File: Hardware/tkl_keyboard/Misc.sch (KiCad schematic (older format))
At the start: 16 parts, among them J6 Conn_01x04_Female, SW90 Rotary_Encoder_Switch, SW91 Rotary_Encoder_Switch, SW92 Rotary_Encoder_Switch

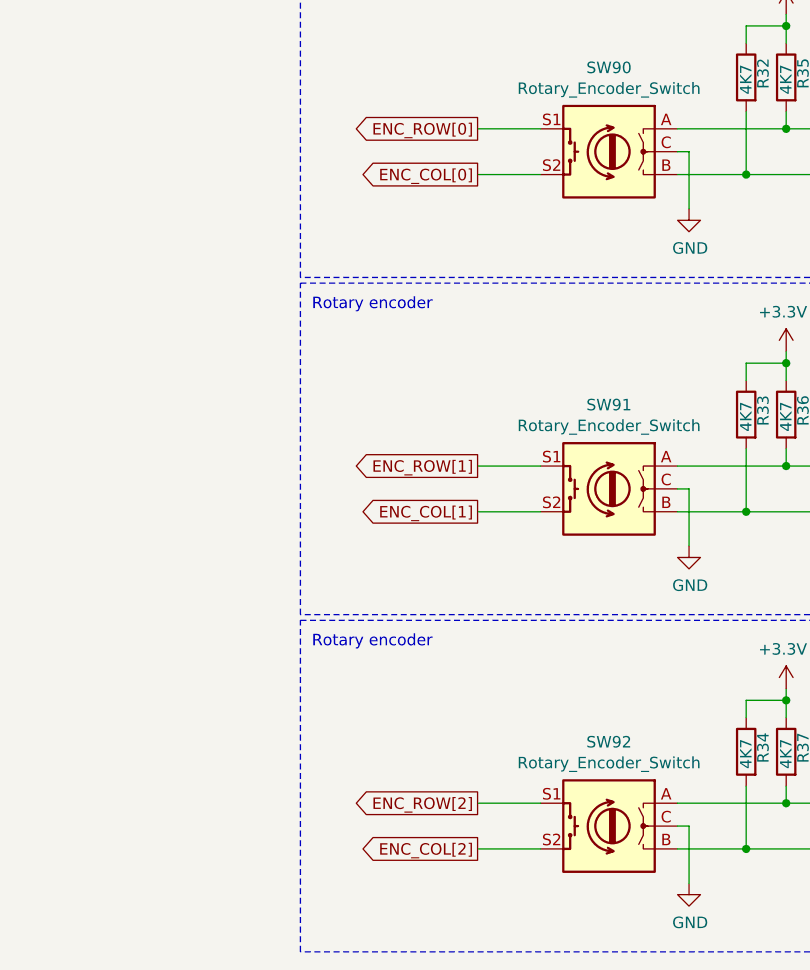
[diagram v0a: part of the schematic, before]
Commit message: LEDs and diodes routed
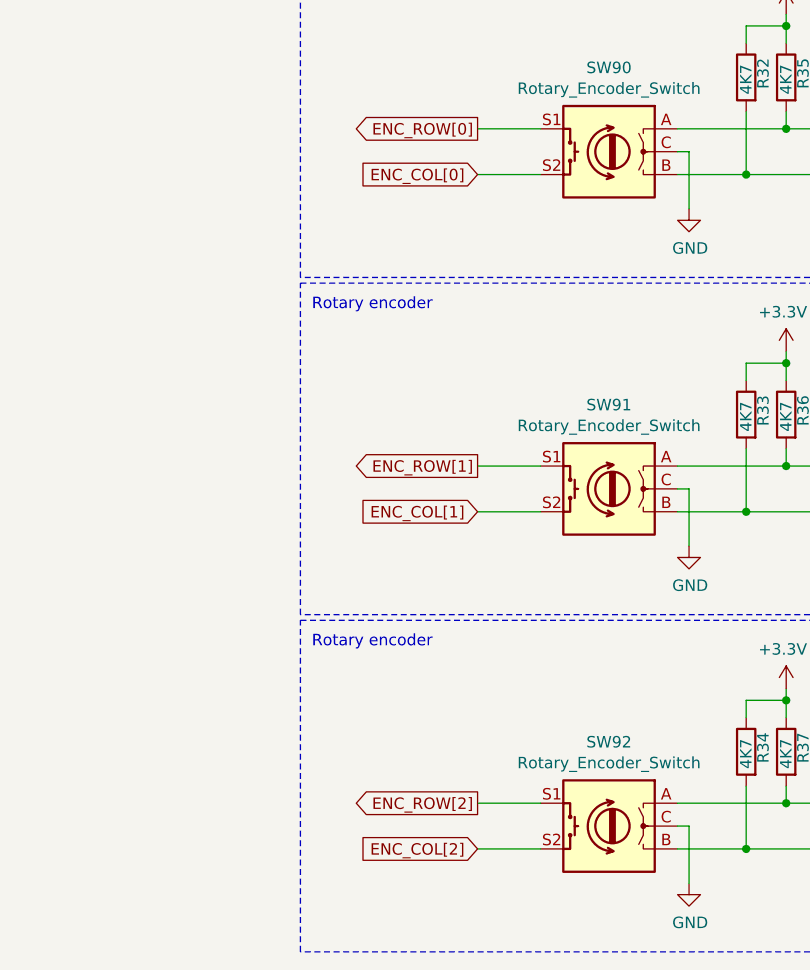
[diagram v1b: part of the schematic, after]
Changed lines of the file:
@@
 Text GLabel 4025 2550 0    50   Output ~ 0
 ENC_ROW[0]
-Text GLabel 4025 2750 0    50   Output ~ 0
+Text GLabel 4025 2750 0    50   Input ~ 0
 ENC_COL[0]
 Wire Wire Line
@@
 Text GLabel 4025 4025 0    50   Output ~ 0
 ENC_ROW[1]
-Text GLabel 4025 4225 0    50   Output ~ 0
+Text GLabel 4025 4225 0    50   Input ~ 0
 ENC_COL[1]
 Wire Wire Line
@@
 Text GLabel 4025 5500 0    50   Output ~ 0
 ENC_ROW[2]
-Text GLabel 4025 5700 0    50   Output ~ 0
+Text GLabel 4025 5700 0    50   Input ~ 0
 ENC_COL[2]
 Wire Wire Line

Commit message: Rows and columns routed to controller. Extended top board edge to fit OLED. Removed optional resistors around CMC.
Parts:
- J6: footprint Connector_PinSocket_2.54mm:PinSocket_1x04_P2.54mm_Vertical -> custom_footprint_library:OLED_128_64
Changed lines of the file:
@@
 F 0 "J6" H 7628 3676 50  0000 L CNN
 F 1 "Conn_01x04_Female" H 7300 3400 50  0000 L CNN
-F 2 "Connector_PinSocket_2.54mm:PinSocket_1x04_P2.54mm_Vertical" H 7600 3700 50  0001 C CNN
+F 2 "custom_footprint_library:OLED_128_64" H 7600 3700 50  0001 C CNN
 F 3 "~" H 7600 3700 50  0001 C CNN
 	1    7600 3700

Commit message: Updating schematic
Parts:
- added H10, H11, H12, H5, H6, H7, H8, H9: MountingHole_Pad, mounting_hole:MountingHole_3.2mm_M3_ISO7380_Pad, symbol Mechanical:MountingHole_Pad
- R32, R33, R34, R35, R36, R37: value 4K7 -> 10K
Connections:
- net GND: now also H10.1, H11.1, H12.1, H5.1, H6.1, H7.1, H8.1, H9.1
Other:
- moved on the sheet: H1, H2, H3, H4, J6, R30, R31, R32, R33, R34, R35, R36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

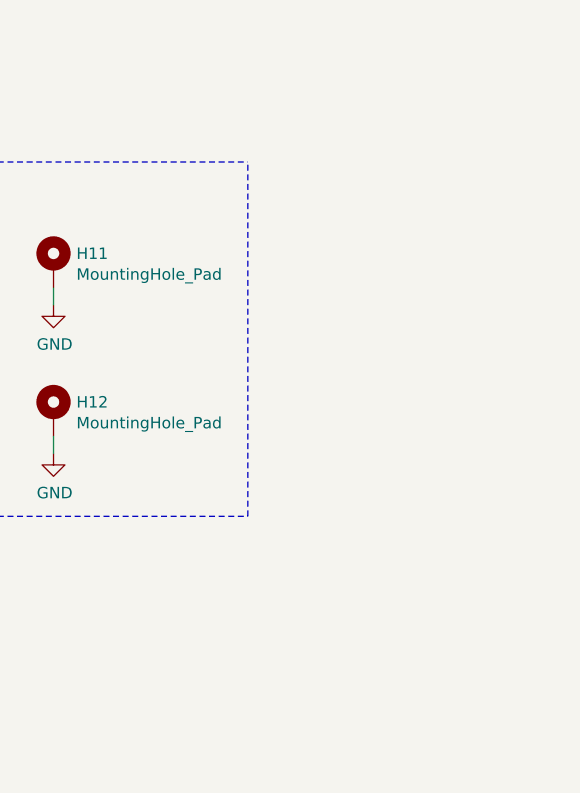
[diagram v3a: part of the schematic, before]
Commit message: First pass of routing done
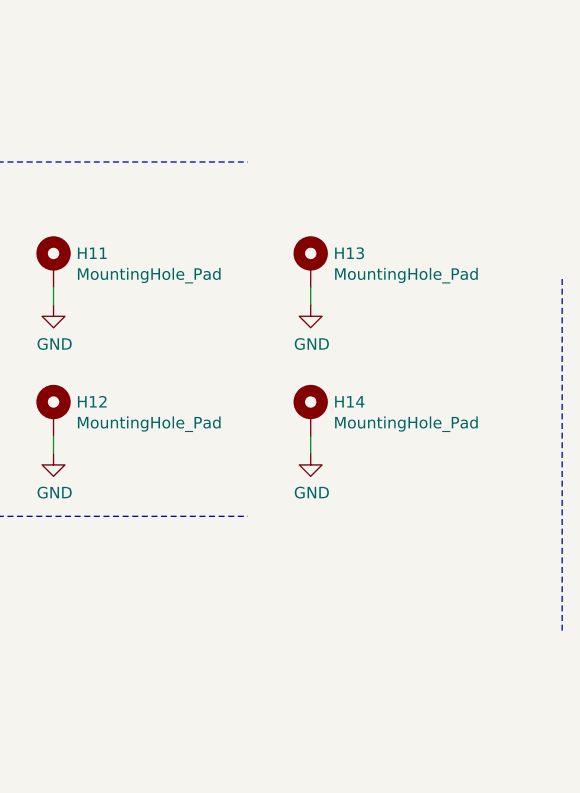
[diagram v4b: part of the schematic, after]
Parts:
- added H13, H14: MountingHole_Pad, mounting_hole:MountingHole_3.2mm_M3_ISO7380_Pad, symbol Mechanical:MountingHole_Pad
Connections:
- net GND: now also H13.1, H14.1
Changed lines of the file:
@@
 	1750 3050 7925 3050
 Wire Notes Line
-	7925 3050 7925 1500
+	9300 3550 9300 2000
 Wire Notes Line
 	1750 1500 7925 1500
+$Comp
+L Mechanical:MountingHole_Pad H?
+U 1 1 61422488
+P 8200 1950
+AR Path="/62F5643B/61422488" Ref="H?"  Part="1"
+AR Path="/63013830/61422488" Ref="H?"  Part="1"
+AR Path="/6301FD9D/61422488" Ref="H?"  Part="1"
+AR Path="/63166CC9/61422488" Ref="H13"  Part="1"
+F 0 "H13" H 8300 1999 50  0000 L CNN
+F 1 "MountingHole_Pad" H 8300 1908 50  0000 L CNN
+F 2 "mounting_hole:MountingHole_3.2mm_M3_ISO7380_Pad" H 8200 1950 50  0001 C CNN
+F 3 "~" H 8200 1950 50  0001 C CNN
+	1    8200 1950
+	1    0    0    -1
+$EndComp
+$Comp
+L power:GND #PWR?
+U 1 1 6142248E
+P 8200 2125
+AR Path="/62F5643B/6142248E" Ref="#PWR?"  Part="1"
+AR Path="/63013830/6142248E" Ref="#PWR?"  Part="1"
+AR Path="/6301FD9D/6142248E" Ref="#PWR?"  Part="1"
+AR Path="/63166CC9/6142248E" Ref="#PWR0529"  Part="1"
+F 0 "#PWR0529" H 8200 1875 50  0001 C CNN
+F 1 "GND" H 8205 1952 50  0000 C CNN
+F 2 "" H 8200 2125 50  0001 C CNN
+F 3 "" H 8200 2125 50  0001 C CNN
+	1    8200 2125
+	1    0    0    -1
+$EndComp
+Wire Wire Line
+	8200 2125 8200 2050
+$Comp
+L Mechanical:MountingHole_Pad H?
+U 1 1 61422495
+P 8200 2600
+AR Path="/62F5643B/61422495" Ref="H?"  Part="1"
+AR Path="/63013830/61422495" Ref="H?"  Part="1"
+AR Path="/6301FD9D/61422495" Ref="H?"  Part="1"
+AR Path="/63166CC9/61422495" Ref="H14"  Part="1"
+F 0 "H14" H 8300 2649 50  0000 L CNN
+F 1 "MountingHole_Pad" H 8300 2558 50  0000 L CNN
+F 2 "mounting_hole:MountingHole_3.2mm_M3_ISO7380_Pad" H 8200 2600 50  0001 C CNN
+F 3 "~" H 8200 2600 50  0001 C CNN
+	1    8200 2600
+	1    0    0    -1
+$EndComp
+$Comp
+L power:GND #PWR?
+U 1 1 6142249B
+P 8200 2775
+AR Path="/62F5643B/6142249B" Ref="#PWR?"  Part="1"
+AR Path="/63013830/6142249B" Ref="#PWR?"  Part="1"
+AR Path="/6301FD9D/6142249B" Ref="#PWR?"  Part="1"
+AR Path="/63166CC9/6142249B" Ref="#PWR0530"  Part="1"
+F 0 "#PWR0530" H 8200 2525 50  0001 C CNN
+F 1 "GND" H 8205 2602 50  0000 C CNN
+F 2 "" H 8200 2775 50  0001 C CNN
+F 3 "" H 8200 2775 50  0001 C CNN
+	1    8200 2775
+	1    0    0    -1
+$EndComp
+Wire Wire Line
+	8200 2775 8200 2700
 $EndSCHEMATC

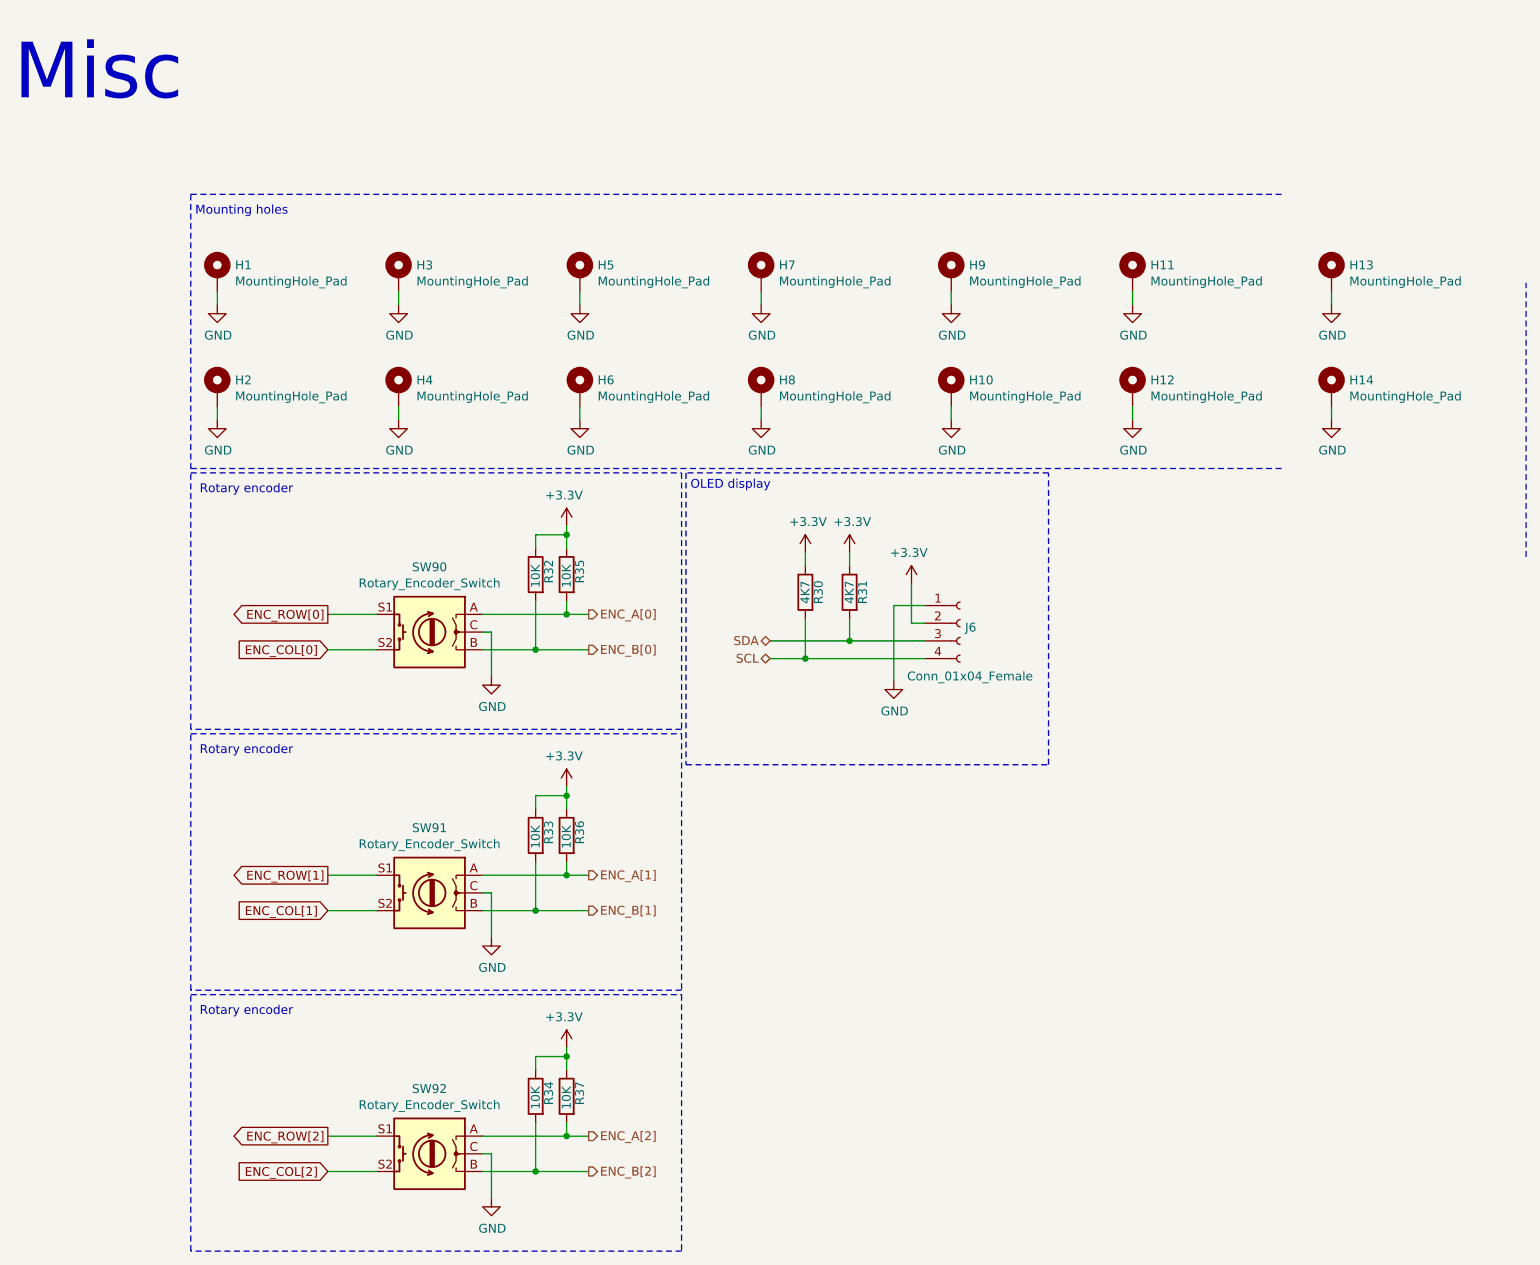
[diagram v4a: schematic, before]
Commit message: Tidying schematic
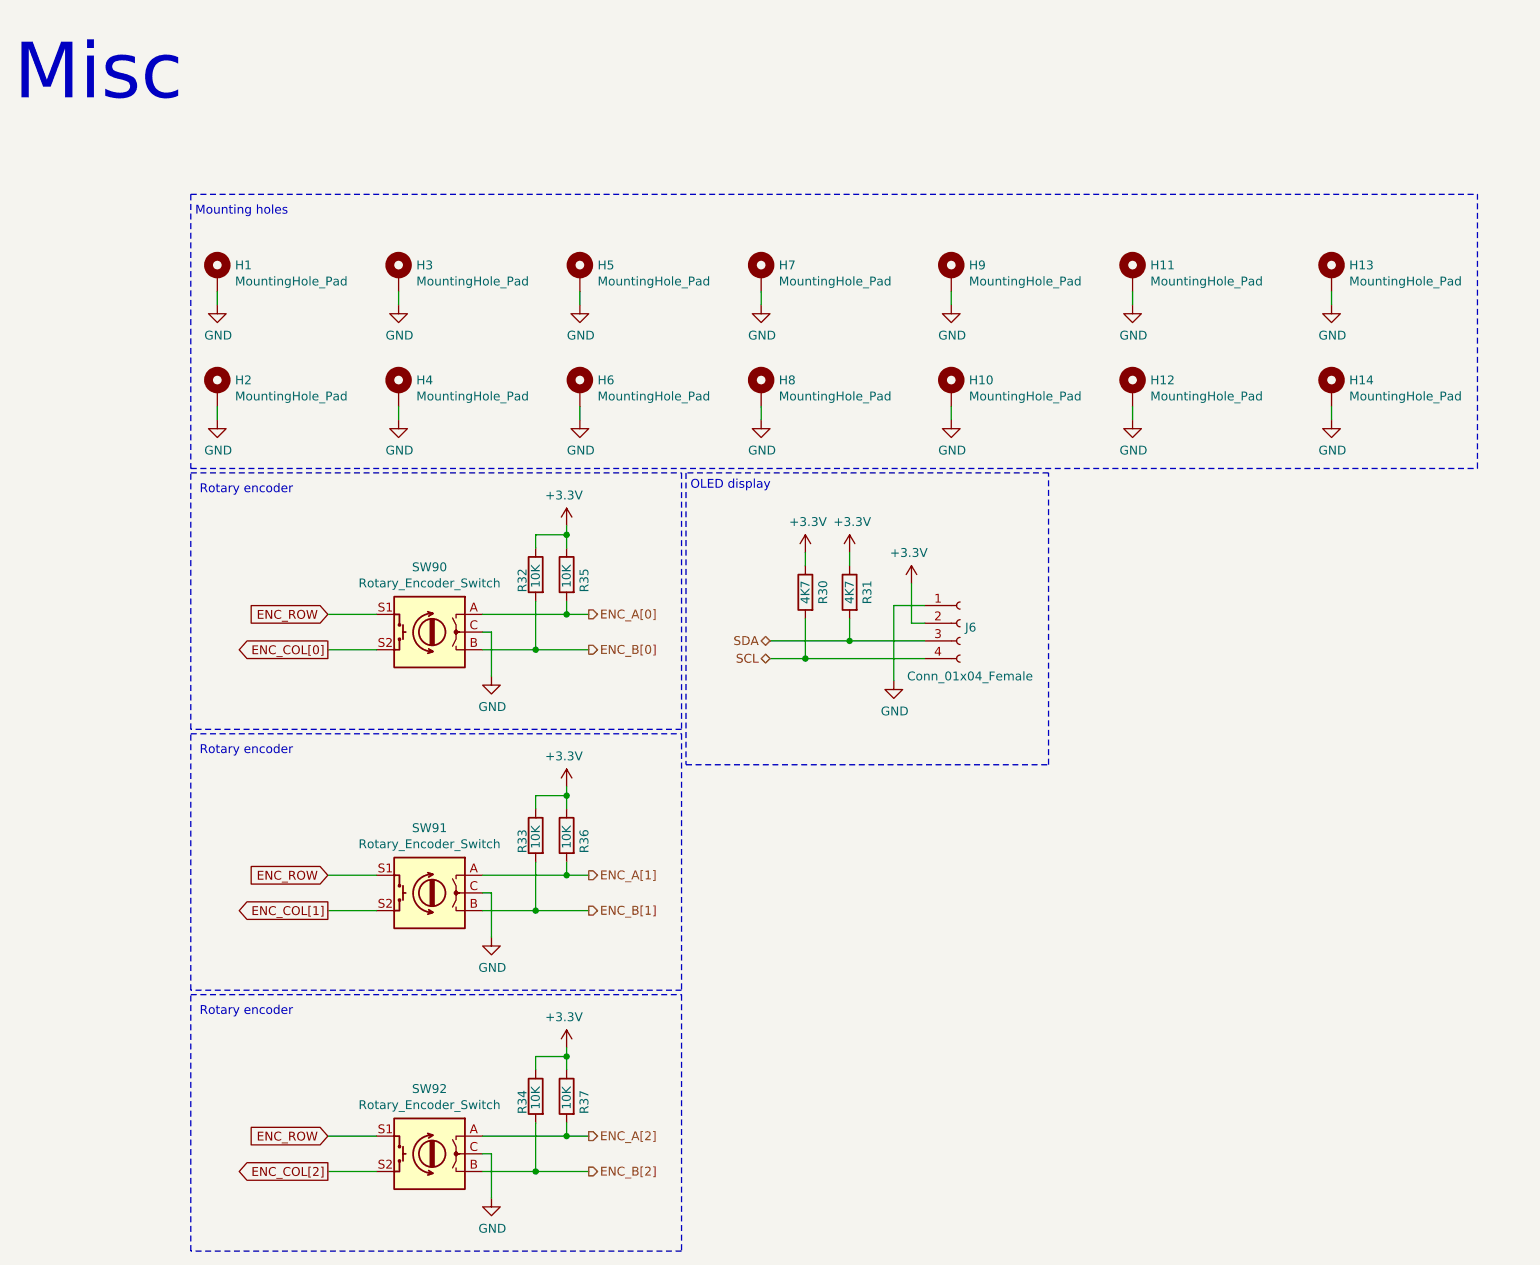
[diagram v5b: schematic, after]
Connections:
- net ENC_ROW[1] is gone; now on net ENC_ROW: SW91.S1
- net ENC_ROW[2] is gone; now on net ENC_ROW: SW92.S1
- net ENC_ROW[0] renamed ENC_ROW
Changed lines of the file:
@@
 encoding utf-8
 Sheet 7 12
-Title ""
+Title "TKL Keyboard"
 Date ""
-Rev ""
+Rev "0"
 Comp ""
 Comment1 ""
@@
 AR Path="/6301FD9D/63210B97" Ref="R?"  Part="1"
 AR Path="/63166CC9/63210B97" Ref="R32"  Part="1"
-F 0 "R32" V 3625 3600 50  0000 L CNN
+F 0 "R32" V 3775 3550 50  0000 L CNN
 F 1 "10K" V 3700 3575 50  0000 L CNN
 F 2 "resistor_smd:R_0603_1608Metric" V 3630 3650 50  0001 C CNN
@@
 AR Path="/6301FD9D/63210B9D" Ref="R?"  Part="1"
 AR Path="/63166CC9/63210B9D" Ref="R35"  Part="1"
-F 0 "R35" V 3800 3600 50  0000 L CNN
+F 0 "R35" V 3775 3550 50  0000 L CNN
 F 1 "10K" V 3875 3575 50  0000 L CNN
 F 2 "resistor_smd:R_0603_1608Metric" V 3805 3650 50  0001 C CNN
@@
 AR Path="/6301FD9D/63210C20" Ref="R?"  Part="1"
 AR Path="/63166CC9/63210C20" Ref="R31"  Part="1"
-F 0 "R31" V 5400 3750 50  0000 C CNN
+F 0 "R31" V 5375 3750 50  0000 C CNN
 F 1 "4K7" V 5475 3750 50  0000 C CNN
 F 2 "resistor_smd:R_0603_1608Metric" V 5405 3750 50  0001 C CNN
@@
 AR Path="/6301FD9D/63210C26" Ref="R?"  Part="1"
 AR Path="/63166CC9/63210C26" Ref="R30"  Part="1"
-F 0 "R30" V 5150 3750 50  0000 C CNN
+F 0 "R30" V 5125 3750 50  0000 C CNN
 F 1 "4K7" V 5225 3750 50  0000 C CNN
 F 2 "resistor_smd:R_0603_1608Metric" V 5155 3750 50  0001 C CNN
@@
 Text HLabel 5025 4125 0    50   BiDi ~ 0
 SCL
-Text GLabel 2525 3875 0    50   Output ~ 0
-ENC_ROW[0]
-Text GLabel 2525 4075 0    50   Input ~ 0
+Text GLabel 2525 3875 0    50   Input ~ 0
+ENC_ROW
+Text GLabel 2525 4075 0    50   Output ~ 0
 ENC_COL[0]
 Wire Wire Line
@@
 AR Path="/6301FD9D/63221704" Ref="R?"  Part="1"
 AR Path="/63166CC9/63221704" Ref="R33"  Part="1"
-F 0 "R33" V 3625 5075 50  0000 L CNN
+F 0 "R33" V 3775 5025 50  0000 L CNN
 F 1 "10K" V 3700 5050 50  0000 L CNN
 F 2 "resistor_smd:R_0603_1608Metric" V 3630 5125 50  0001 C CNN
@@
 AR Path="/6301FD9D/6322170A" Ref="R?"  Part="1"
 AR Path="/63166CC9/6322170A" Ref="R36"  Part="1"
-F 0 "R36" V 3800 5075 50  0000 L CNN
+F 0 "R36" V 3775 5025 50  0000 L CNN
 F 1 "10K" V 3875 5050 50  0000 L CNN
 F 2 "resistor_smd:R_0603_1608Metric" V 3805 5125 50  0001 C CNN
@@
 Wire Notes Line
 	1750 6000 1750 4550
-Text GLabel 2525 5350 0    50   Output ~ 0
-ENC_ROW[1]
-Text GLabel 2525 5550 0    50   Input ~ 0
+Text GLabel 2525 5550 0    50   Output ~ 0
 ENC_COL[1]
 Wire Wire Line
@@
 AR Path="/6301FD9D/63223F26" Ref="R?"  Part="1"
 AR Path="/63166CC9/63223F26" Ref="R34"  Part="1"
-F 0 "R34" V 3625 6550 50  0000 L CNN
+F 0 "R34" V 3775 6500 50  0000 L CNN
 F 1 "10K" V 3700 6525 50  0000 L CNN
 F 2 "resistor_smd:R_0603_1608Metric" V 3630 6600 50  0001 C CNN
@@
 AR Path="/6301FD9D/63223F2C" Ref="R?"  Part="1"
 AR Path="/63166CC9/63223F2C" Ref="R37"  Part="1"
-F 0 "R37" V 3800 6550 50  0000 L CNN
+F 0 "R37" V 3775 6500 50  0000 L CNN
 F 1 "10K" V 3875 6525 50  0000 L CNN
 F 2 "resistor_smd:R_0603_1608Metric" V 3805 6600 50  0001 C CNN
@@
 Wire Notes Line
 	1750 7475 1750 6025
-Text GLabel 2525 6825 0    50   Output ~ 0
-ENC_ROW[2]
-Text GLabel 2525 7025 0    50   Input ~ 0
+Text GLabel 2525 7025 0    50   Output ~ 0
 ENC_COL[2]
 Wire Wire Line
@@
 Wire Notes Line
 	1750 1500 1750 3050
-Wire Notes Line
-	1750 3050 7925 3050
-Wire Notes Line
-	9300 3550 9300 2000
-Wire Notes Line
-	1750 1500 7925 1500
 $Comp
 L Mechanical:MountingHole_Pad H?
@@
 Wire Wire Line
 	8200 2775 8200 2700
+Wire Notes Line
+	9025 3050 9025 1500
+Wire Notes Line
+	1750 3050 9025 3050
+Wire Notes Line
+	1750 1500 9025 1500
+Text GLabel 2525 5350 0    50   Input ~ 0
+ENC_ROW
+Text GLabel 2525 6825 0    50   Input ~ 0
+ENC_ROW
 $EndSCHEMATC
